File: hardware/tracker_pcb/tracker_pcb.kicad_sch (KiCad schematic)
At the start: 32 parts, among them J1 1751196, J2 B6B-PH-K-S, J3 1713286, J5 B4B-XH-A, J6 Screw_Terminal_01x02, U2 SN74AUP2G125YZPR, U8 SN74AUP2G125YZPR

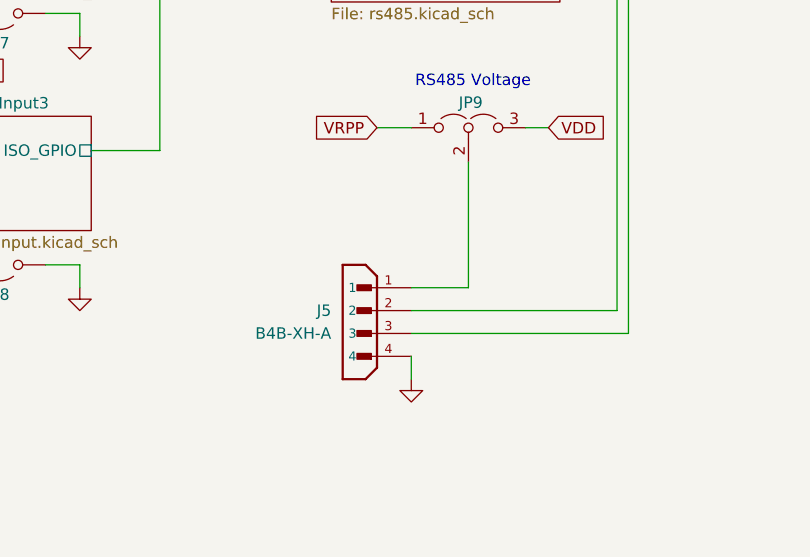
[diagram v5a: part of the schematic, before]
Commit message: Dual rs485 connectors
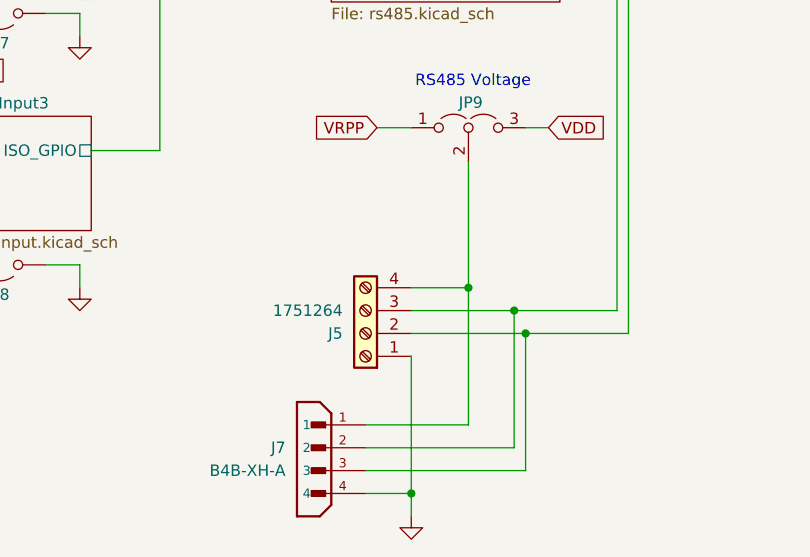
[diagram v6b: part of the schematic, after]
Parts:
- removed J5: B4B-XH-A, footprint:JST_B4B-XH-A, symbol symbol:B4B-XH-A
- added J5: 1751264, footprint:PHOENIX_1751264, symbol symbol:1751264
- added J7: B4B-XH-A, footprint:JST_B4B-XH-A, symbol symbol:B4B-XH-A
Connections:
- net GND: now also J5.1, J7.4
- net RS485/A: now also J5.3, J7.2
- net RS485/B: now also J5.2, J7.3
- net at JP9.2 (C): now also J5.4, J7.1

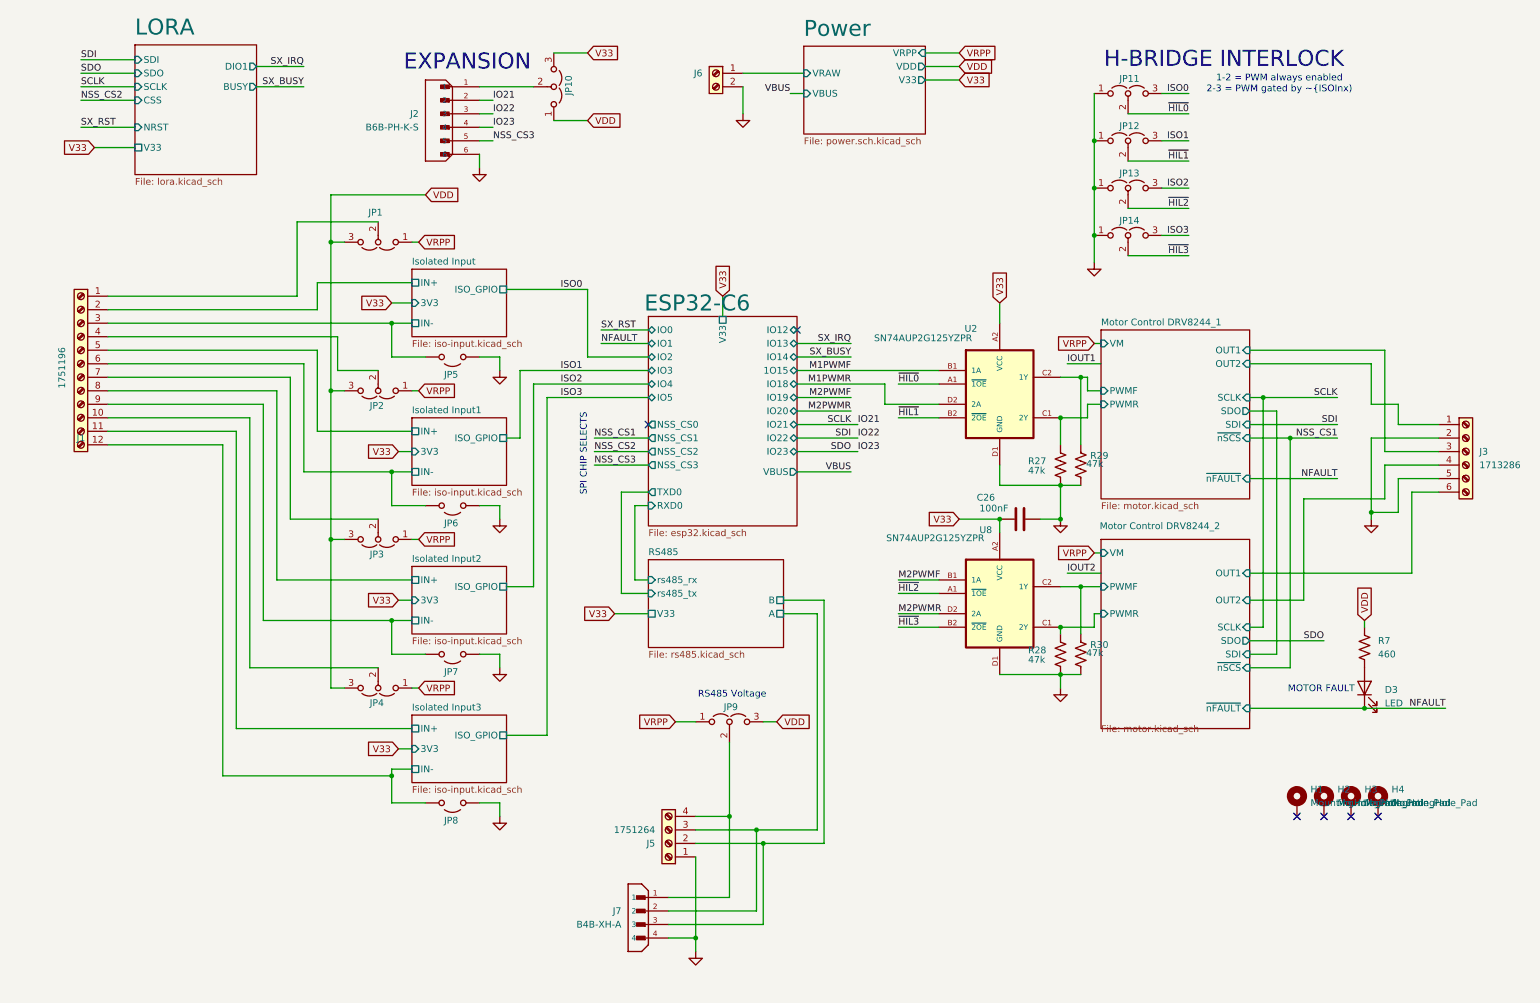
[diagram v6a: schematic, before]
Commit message: Beef up 5v supply and add new power mux
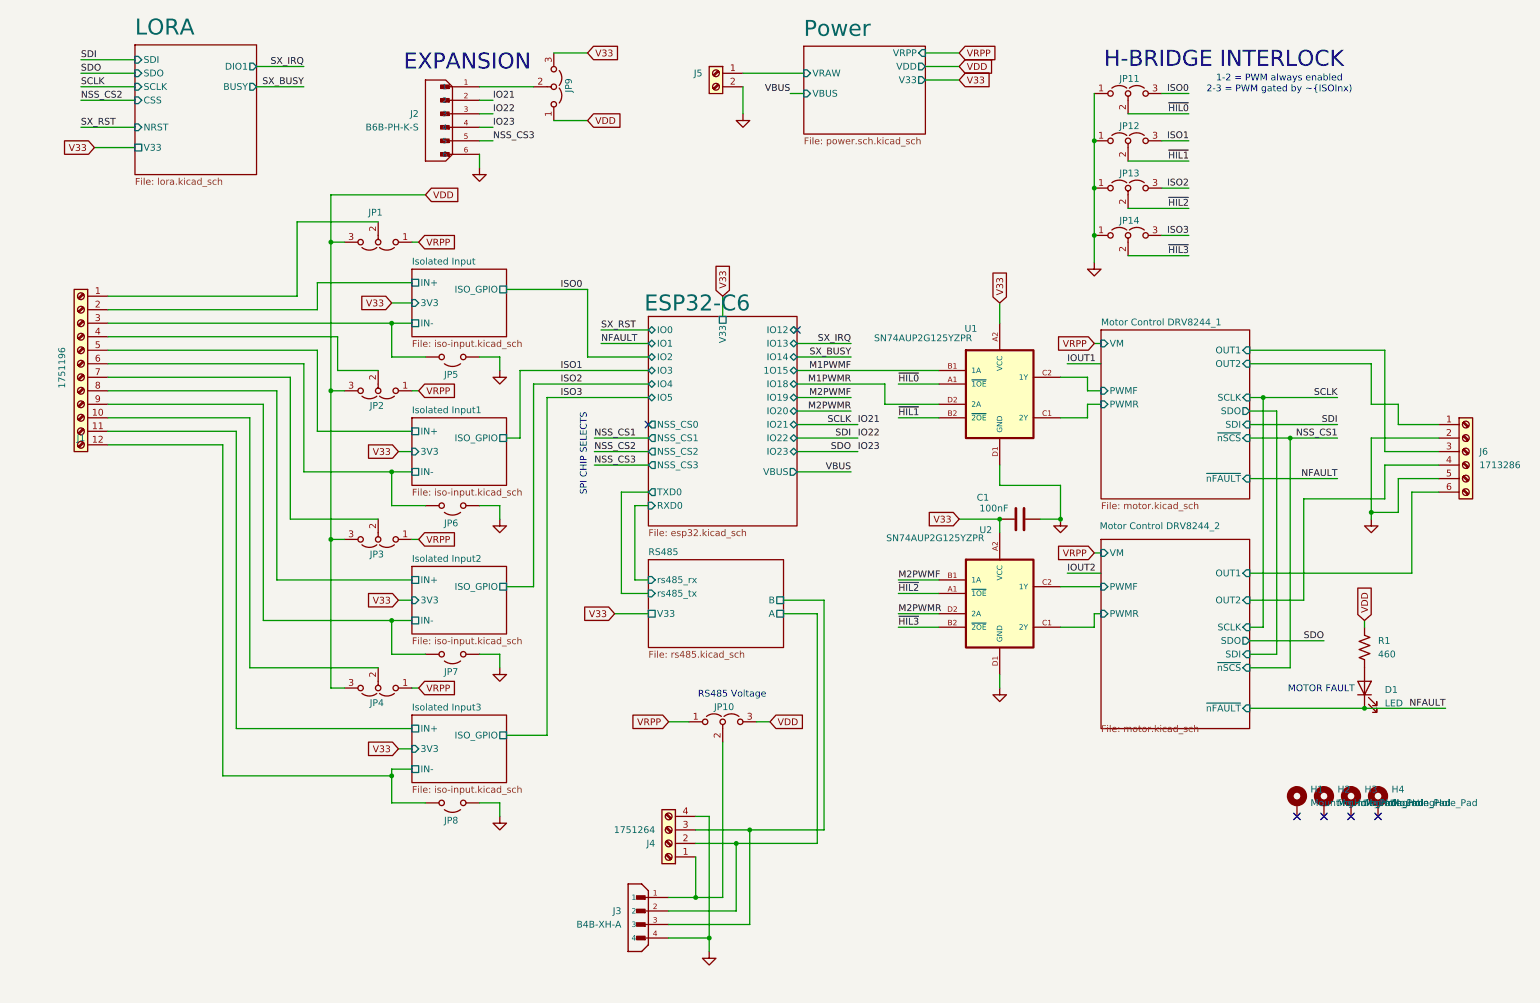
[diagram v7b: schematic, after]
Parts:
- removed R27, R28, R29, R30: 47k, Resistor_SMD:R_0603_1608Metric, symbol Device:R_US
- renumbered C26 to C1, D3 to D1, J7 to J3, J5 to J4, J6 to J5, J3 to J6, JP9 to JP10, JP10 to JP9, R7 to R1, U2 to U1, U8 to U2
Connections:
- net GND: now also J4.4; no longer J4.1
- net RS485/A: now also J4.2; no longer J4.3
- net RS485/B: now also J4.3; no longer J4.2
- net at J3.1, JP10.2 (C): now also J4.1; no longer J4.4
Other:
- moved on the sheet: JP10

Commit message: Modify iso circuit for best CTR
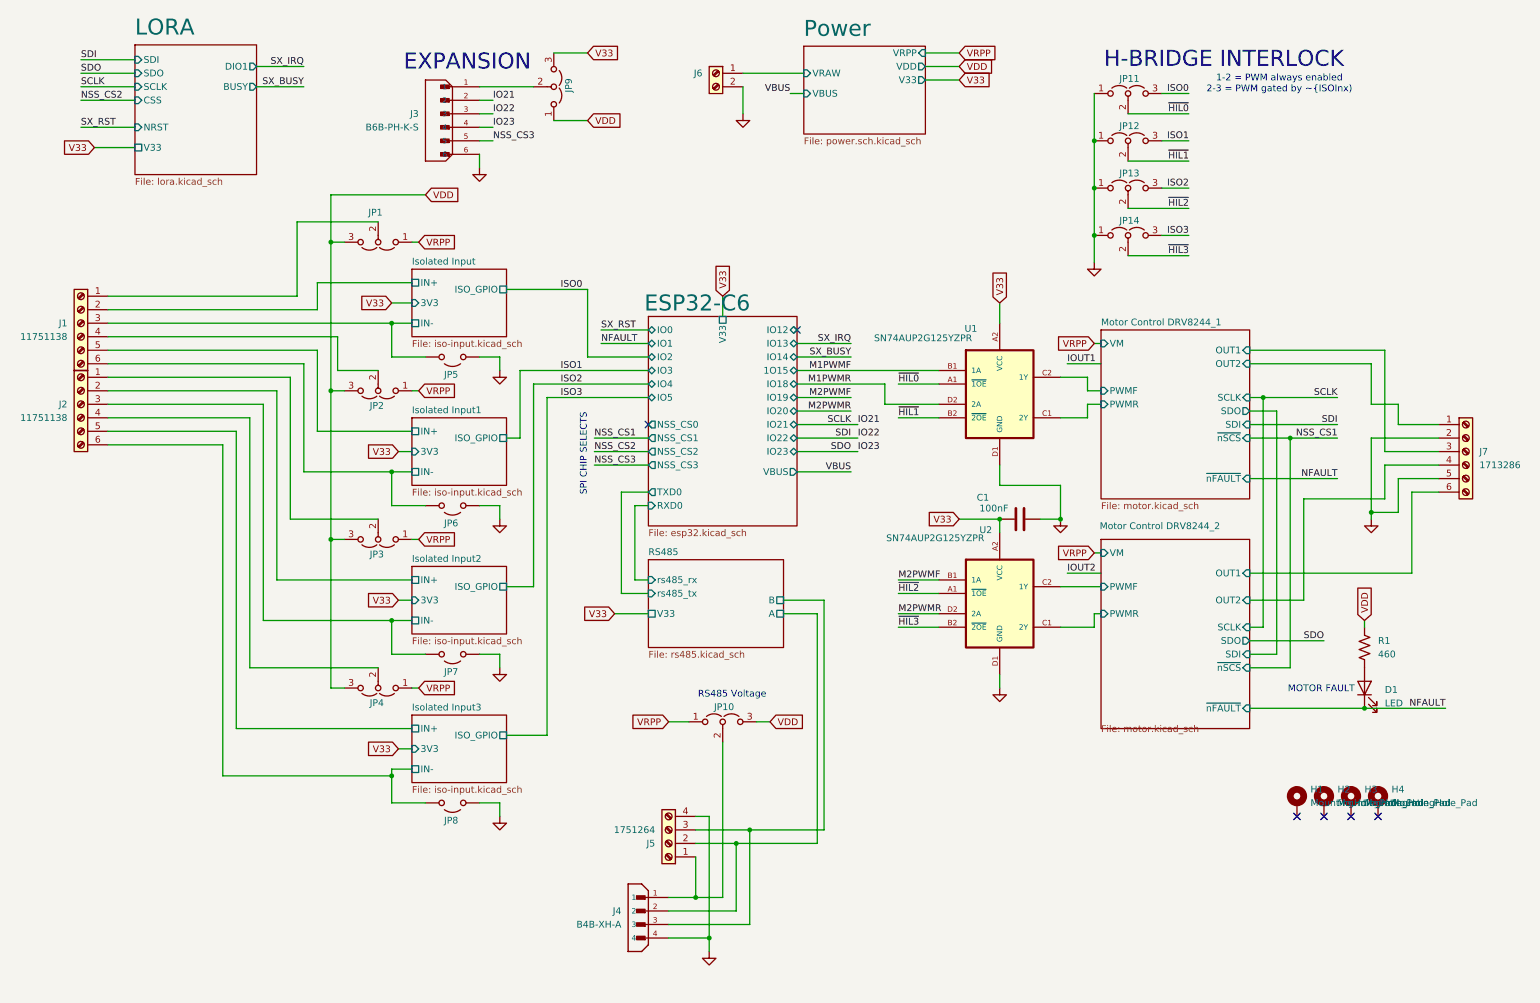
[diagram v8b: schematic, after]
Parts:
- removed J1: 1751196, footprint:CONN_1751196, symbol Connector:Screw_Terminal_01x12
- added J1, J2: 11751138, footprint:CONN_1751138_PXC, symbol Connector:Screw_Terminal_01x06
- J7: renamed from J6; LCSC C6366609 -> C2997523
- renumbered J2 to J3, J3 to J4, J4 to J5, J5 to J6
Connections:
- net Isolated Input/IN+: now also J1.2 (Pin_2)
- net Isolated Input/IN-: now also J1.3 (Pin_3)
- net Isolated Input1/IN+: now also J1.5 (Pin_5)
- net Isolated Input1/IN-: now also J1.6 (Pin_6)
- net Isolated Input2/IN+: now also J2.2 (Pin_2)
- net Isolated Input2/IN-: now also J2.3 (Pin_3)
- net Isolated Input3/IN+: now also J2.5 (Pin_5)
- net Isolated Input3/IN-: now also J2.6 (Pin_6)
- net at JP4.2 (C): now also J2.4 (Pin_4)
- net at JP3.2 (C): now also J2.1 (Pin_1)
- net at JP1.2 (C): now also J1.1 (Pin_1)
- net at JP2.2 (C): now also J1.4 (Pin_4)
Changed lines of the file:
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@@
+	)
+	(symbol
+		(lib_id "Connector:Screw_Terminal_01x06")
+		(at 17.78 86.36 0)
+		(mirror y)
+		(unit 1)
+		(exclude_from_sim no)
+		(in_bom yes)
+		(on_board yes)
+		(dnp no)
+		(property "Reference" "J2"
+			(at 15.24 86.3599 0)
+			(effects
+				(font
+					(size 1.27 1.27)
+				)
+				(justify left)
+			)
+		)
+		(property "Value" "11751138"
+			(at 15.24 88.8999 0)
+			(effects
+				(font
+					(size 1.27 1.27)
+				)
+				(justify left)
+			)
+		)
+		(property "Footprint" "footprint:CONN_1751138_PXC"
+			(at 17.78 86.36 0)
+			(effects
+				(font
+					(size 1.27 1.27)
+				)
+				(hide yes)
+			)
+		)
+		(property "Datasheet" "~"
+			(at 17.78 86.36 0)
+			(effects
+				(font
+					(size 1.27 1.27)
+				)
+				(hide yes)
+			)
+		)
+		(property "Description" "Generic screw terminal, single row, 01x06, script generated (kicad-library-utils/schlib/autogen/connector/)"
+			(at 17.78 86.36 0)
+			(effects
+				(font
+					(size 1.27 1.27)
+				)
+				(hide yes)
+			)
+		)
+		(property "LCSC" "C2997513"
+			(at 17.78 86.36 0)
+			(effects
+				(font
+					(size 1.27 1.27)
+				)
+				(hide yes)
+			)
+		)
+		(pin "2"
+		)
+		(pin "3"
+		)
+		(pin "4"
+		)
+		(pin "5"
+		)
+		(pin "6"
+		)
+		(pin "1"
+		)
+		(instances
+			(project "tracker_pcb"
+				(path "/6aaa9514-f94e-4843-90d0-16960e4e49cb"
+					(reference "J2")
+					(unit 1)
+				)
+			)
+		)
 	)
 	(symbol
@@
 		(on_board yes)
 		(dnp no)
-		(property "Reference" "J3"
+		(property "Reference" "J4"
 			(at 119.38 181.6099 0)
 			(effects
@@
 			(project ""
 				(path "/6aaa9514-f94e-4843-90d0-16960e4e49cb"
-					(reference "J3")
+					(reference "J4")
 					(unit 1)
 				)
@@
 		(on_board yes)
 		(dnp no)
-		(property "Reference" "J4"
+		(property "Reference" "J5"
 			(at 125.73 168.9101 0)
 			(effects
@@
 			(project "tracker_pcb"
 				(path "/6aaa9514-f94e-4843-90d0-16960e4e49cb"
-					(reference "J4")
+					(reference "J5")
 					(unit 1)
 				)
@@
 		(on_board yes)
 		(dnp no)
-		(property "Reference" "J2"
+		(property "Reference" "J3"
 			(at 81.28 31.7499 0)
 			(effects
@@
 			(project ""
 				(path "/6aaa9514-f94e-4843-90d0-16960e4e49cb"
-					(reference "J2")
+					(reference "J3")
 					(unit 1)
 				)
@@
 	)
 	(symbol
-		(lib_id "Connector:Screw_Terminal_01x12")
-		(at 17.78 78.74 0)
+		(lib_id "Connector:Screw_Terminal_01x06")
+		(at 17.78 71.12 0)
 		(mirror y)
 		(unit 1)
@@
 		(dnp no)
 		(property "Reference" "J1"
-			(at 17.78 92.71 0)
-			(effects
-				(font
-					(size 1.27 1.27)
-				)
-			)
-		)
-		(property "Value" "1751196"
-			(at 14.224 79.502 90)
-			(effects
-				(font
-					(size 1.27 1.27)
-				)
-			)
-		)
-		(property "Footprint" "footprint:CONN_1751196"
-			(at 17.78 78.74 0)
+			(at 15.24 71.1199 0)
+			(effects
+				(font
+					(size 1.27 1.27)
+				)
+				(justify left)
+			)
+		)
+		(property "Value" "11751138"
+			(at 15.24 73.6599 0)
+			(effects
+				(font
+					(size 1.27 1.27)
+				)
+				(justify left)
+			)
+		)
+		(property "Footprint" "footprint:CONN_1751138_PXC"
+			(at 17.78 71.12 0)
 			(effects
 				(font
@@
 		)
 		(property "Datasheet" "~"
-			(at 17.78 78.74 0)
-			(effects
-				(font
-					(size 1.27 1.27)
-				)
-				(hide yes)
-			)
-		)
-		(property "Description" "Generic screw terminal, single row, 01x12, script generated (kicad-library-utils/schlib/autogen/connector/)"
-			(at 17.78 78.74 0)
-			(effects
-				(font
-					(size 1.27 1.27)
-				)
-				(hide yes)
-			)
-		)
-		(property "LCSC" "C7164425"
-			(at 17.78 92.71 0)
-			(effects
-				(font
-					(size 1.27 1.27)
-				)
-				(hide yes)
-			)
+			(at 17.78 71.12 0)
+			(effects
+				(font
+					(size 1.27 1.27)
+				)
+				(hide yes)
+			)
+		)
+		(property "Description" "Generic screw terminal, single row, 01x06, script generated (kicad-library-utils/schlib/autogen/connector/)"
+			(at 17.78 71.12 0)
+			(effects
+				(font
+					(size 1.27 1.27)
+				)
+				(hide yes)
+			)
+		)
+		(property "LCSC" "C2997513"
+			(at 17.78 71.12 0)
+			(effects
+				(font
+					(size 1.27 1.27)
+				)
+				(hide yes)
+			)
+		)
+		(pin "2"
+		)
+		(pin "3"
+		)
+		(pin "4"
+		)
+		(pin "5"
 		)
 		(pin "6"
 		)
-		(pin "5"
-		)
-		(pin "2"
-		)
-		(pin "1"
-		)
-		(pin "3"
-		)
-		(pin "4"
-		)
-		(pin "9"
-		)
-		(pin "8"
-		)
-		(pin "7"
-		)
-		(pin "10"
-		)
-		(pin "11"
-		)
-		(pin "12"
-		)
-		(instances
-			(project "tracker_pcb"
+		(pin "1"
+		)
+		(instances
+			(project ""
 				(path "/6aaa9514-f94e-4843-90d0-16960e4e49cb"
 					(reference "J1")
@@
 		(dnp no)
 		(fields_autoplaced yes)
-		(property "Reference" "J6"
+		(property "Reference" "J7"
 			(at 280.67 95.2499 0)
 			(effects
@@
 			)
 		)
-		(property "LCSC" "C6366609"
+		(property "LCSC" "C2997523"
 			(at 278.13 95.25 0)
 			(effects
@@
 			(project ""
 				(path "/6aaa9514-f94e-4843-90d0-16960e4e49cb"
-					(reference "J6")
+					(reference "J7")
 					(unit 1)
 				)
@@
 		(on_board yes)
 		(dnp no)
-		(property "Reference" "J5"
+		(property "Reference" "J6"
 			(at 134.62 24.1299 0)
 			(effects
@@
 			(project ""
 				(path "/6aaa9514-f94e-4843-90d0-16960e4e49cb"
-					(reference "J5")
-					(unit 1)
-				)
+					(reference "J6")
+					(unit 1)
+				)
